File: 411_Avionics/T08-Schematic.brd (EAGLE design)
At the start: 61.7 x 25.4 mm, 41 parts, among them IC1 BQ24022, J1 USB-MICROB, J3 JST-PH-2-SMT-RA, U1 LP5907, U2 M25P10-AVMN6TP_TR, U3 LSM9DS0, U5 LTC1998, U6 ATMEGA32U4-AU, X1 8MHz

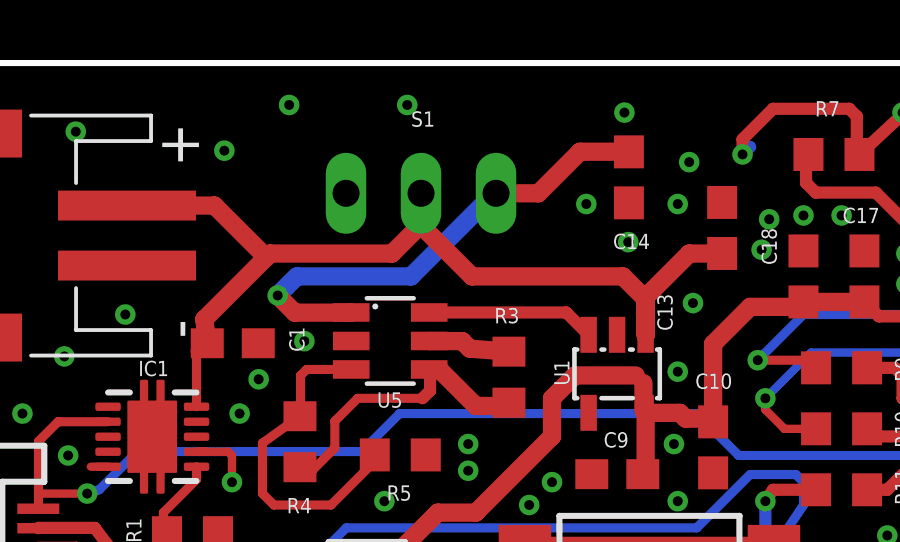
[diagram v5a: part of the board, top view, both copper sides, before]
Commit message: Updated a few oopsies on board layout.  A couple nodes not connected, switch on bottom layer.  Added a couple more vias as well.
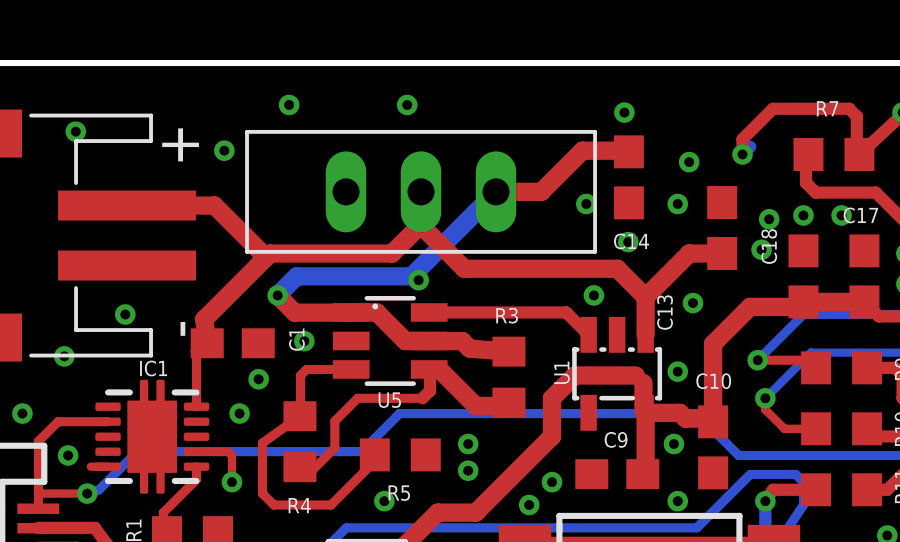
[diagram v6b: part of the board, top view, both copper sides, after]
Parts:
- flipped S1 to the top, turned to 0 degrees
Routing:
- net N$15: track 19.2 -> 22.2 mm
- net GND: vias 78 -> 80
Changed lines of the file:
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@@
 <layers>
 <layer number="1" name="Top" color="4" fill="1" visible="yes" active="yes"/>
-<layer number="16" name="Bottom" color="1" fill="1" visible="yes" active="yes"/>
+<layer number="16" name="Bottom" color="1" fill="1" visible="no" active="yes"/>
 <layer number="17" name="Pads" color="2" fill="1" visible="yes" active="yes"/>
 <layer number="18" name="Vias" color="2" fill="1" visible="yes" active="yes"/>
@@
 <layer number="20" name="Dimension" color="15" fill="1" visible="yes" active="yes"/>
 <layer number="21" name="tPlace" color="7" fill="1" visible="yes" active="yes"/>
-<layer number="22" name="bPlace" color="7" fill="1" visible="yes" active="yes"/>
+<layer number="22" name="bPlace" color="7" fill="1" visible="no" active="yes"/>
 <layer number="23" name="tOrigins" color="15" fill="1" visible="yes" active="yes"/>
-<layer number="24" name="bOrigins" color="15" fill="1" visible="yes" active="yes"/>
+<layer number="24" name="bOrigins" color="15" fill="1" visible="no" active="yes"/>
 <layer number="25" name="tNames" color="7" fill="1" visible="no" active="yes"/>
 <layer number="26" name="bNames" color="7" fill="1" visible="no" active="yes"/>
@@
 <layer number="50" name="dxf" color="7" fill="1" visible="no" active="no"/>
 <layer number="51" name="tDocu" color="7" fill="1" visible="yes" active="yes"/>
-<layer number="52" name="bDocu" color="7" fill="1" visible="yes" active="yes"/>
+<layer number="52" name="bDocu" color="7" fill="1" visible="no" active="yes"/>
 <layer number="53" name="tGND_GNDA" color="7" fill="9" visible="no" active="no"/>
 <layer number="54" name="bGND_GNDA" color="1" fill="9" visible="no" active="no"/>
@@
 <attribute name="NAME" x="34.29" y="15.605" size="0.508" layer="25" rot="R270"/>
 </element>
-<element name="S1" library="tinyav-lib" package="ESWITCH" value="COM-00102" x="18.494" y="21.058" smashed="yes" rot="MR180">
-<attribute name="NAME" x="18.161" y="23.279" size="0.508" layer="25" font="vector"/>
+<element name="S1" library="tinyav-lib" package="ESWITCH" value="COM-00102" x="18.494" y="21.106" smashed="yes">
+<attribute name="NAME" x="18.161" y="18.885" size="0.508" layer="26" font="vector" rot="MR180"/>
 </element>
 <element name="S2" library="switch-ck" package="PTS645-SMD" value="PTS645SM43SMTR92" x="26.108" y="7.056" smashed="yes" rot="R180">
@@
 <via x="27.432" y="22.098" extent="1-16" drill="0.3302"/>
 <via x="25.4" y="19.431" extent="1-16" drill="0.3302"/>
+<via x="18.415" y="18.161" extent="1-16" drill="0.3302"/>
+<via x="24.257" y="17.653" extent="1-16" drill="0.3302"/>
 </signal>
 <signal name="N$4">
@@
 <wire x1="11.608" y1="20.65" x2="13.335" y2="18.923" width="0.6096" layer="1"/>
 <wire x1="11.011" y1="13.944" x2="11.011" y2="15.803" width="0.3048" layer="1"/>
-<wire x1="17.526" y1="19.05" x2="18.542" y2="20.066" width="0.6096" layer="1"/>
-<wire x1="18.542" y1="20.066" x2="18.542" y2="21.01" width="0.6096" layer="1"/>
-<wire x1="18.542" y1="21.01" x2="18.494" y2="21.058" width="0.6096" layer="1"/>
-<wire x1="18.542" y1="20.066" x2="18.542" y2="19.939" width="0.6096" layer="1"/>
-<wire x1="18.542" y1="19.939" x2="20.193" y2="18.288" width="0.6096" layer="1"/>
-<wire x1="20.193" y1="18.288" x2="25.222" y2="18.288" width="0.6096" layer="1"/>
-<wire x1="25.222" y1="18.288" x2="25.983" y2="17.527" width="0.6096" layer="1"/>
-<wire x1="25.983" y1="17.527" x2="25.983" y2="16.343" width="0.6096" layer="1"/>
-<wire x1="25.983" y1="16.343" x2="25.98" y2="16.34" width="0.6096" layer="1"/>
 <wire x1="25.98" y1="16.34" x2="25.98" y2="17.598" width="0.6096" layer="1"/>
 <wire x1="25.98" y1="17.598" x2="27.432" y2="19.05" width="0.6096" layer="1"/>
 <wire x1="27.432" y1="19.05" x2="28.53" y2="19.05" width="0.6096" layer="1"/>
 <wire x1="28.53" y1="19.05" x2="28.532" y2="19.052" width="0.6096" layer="1"/>
+<wire x1="18.494" y1="21.106" x2="18.494" y2="20.018" width="0.6096" layer="1"/>
+<wire x1="18.494" y1="20.018" x2="17.526" y2="19.05" width="0.6096" layer="1"/>
+<wire x1="18.494" y1="21.106" x2="18.494" y2="19.987" width="0.6096" layer="1"/>
+<wire x1="18.494" y1="19.987" x2="19.939" y2="18.542" width="0.6096" layer="1"/>
+<wire x1="19.939" y1="18.542" x2="25.036" y2="18.542" width="0.6096" layer="1"/>
+<wire x1="25.036" y1="18.542" x2="25.98" y2="17.598" width="0.6096" layer="1"/>
 </signal>
 <signal name="N$12">
@@
 <wire x1="19.866" y1="16.132" x2="18.772" y2="16.132" width="0.6096" layer="1"/>
 <wire x1="18.772" y1="16.132" x2="18.768" y2="16.136" width="0.6096" layer="1"/>
-<wire x1="20.994" y1="21.058" x2="20.931" y2="21.058" width="0.6096" layer="16"/>
-<wire x1="20.931" y1="21.058" x2="18.161" y2="18.288" width="0.6096" layer="16"/>
-<wire x1="18.161" y1="18.288" x2="14.351" y2="18.288" width="0.6096" layer="16"/>
+<wire x1="18.176" y1="18.288" x2="14.351" y2="18.288" width="0.6096" layer="16"/>
 <wire x1="14.351" y1="18.288" x2="13.716" y2="17.653" width="0.6096" layer="16"/>
 <via x="13.716" y="17.653" extent="1-16" drill="0.3302"/>
@@
 <wire x1="14.284" y1="17.08" x2="16.162" y2="17.08" width="0.6096" layer="1"/>
 <wire x1="16.162" y1="17.08" x2="16.168" y2="17.086" width="0.6096" layer="1"/>
-<wire x1="20.994" y1="21.058" x2="22.406" y2="21.058" width="0.6096" layer="1"/>
-<wire x1="22.406" y1="21.058" x2="23.792" y2="22.444" width="0.6096" layer="1"/>
-<wire x1="23.792" y1="22.444" x2="25.419" y2="22.444" width="0.6096" layer="1"/>
 <wire x1="25.419" y1="22.444" x2="25.423" y2="22.44" width="0.6096" layer="1"/>
-<wire x1="18.161" y1="18.288" x2="18.772" y2="16.132" width="0" layer="19" extent="1-16"/>
+<wire x1="18.772" y1="16.132" x2="17.975" y2="16.132" width="0.6096" layer="1"/>
+<wire x1="17.975" y1="16.132" x2="17.02" y2="17.087" width="0.6096" layer="1"/>
+<wire x1="17.02" y1="17.087" x2="16.169" y2="17.087" width="0.6096" layer="1"/>
+<wire x1="16.169" y1="17.087" x2="16.168" y2="17.086" width="0.6096" layer="1"/>
+<wire x1="20.994" y1="21.106" x2="22.503" y2="21.106" width="0.6096" layer="1"/>
+<wire x1="22.503" y1="21.106" x2="23.876" y2="22.479" width="0.6096" layer="1"/>
+<wire x1="23.876" y1="22.479" x2="25.384" y2="22.479" width="0.6096" layer="1"/>
+<wire x1="25.384" y1="22.479" x2="25.423" y2="22.44" width="0.6096" layer="1"/>
+<wire x1="18.176" y1="18.288" x2="20.994" y2="21.106" width="0.6096" layer="16"/>
 </signal>
 <signal name="RED_LED">

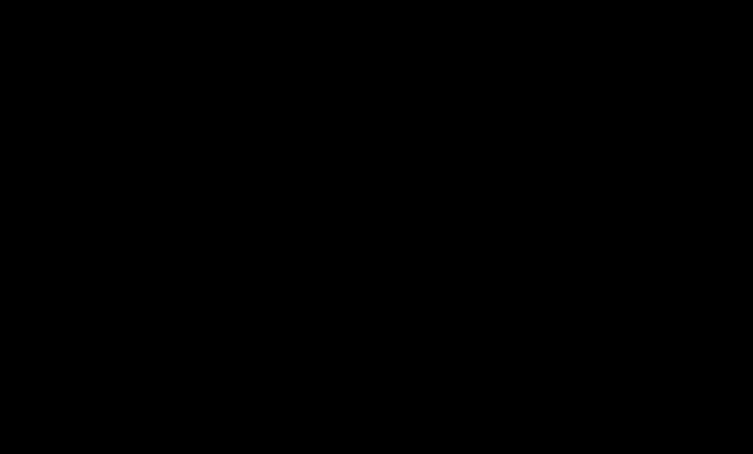
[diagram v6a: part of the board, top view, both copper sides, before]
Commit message: Added 3-pin pad for firing circuit
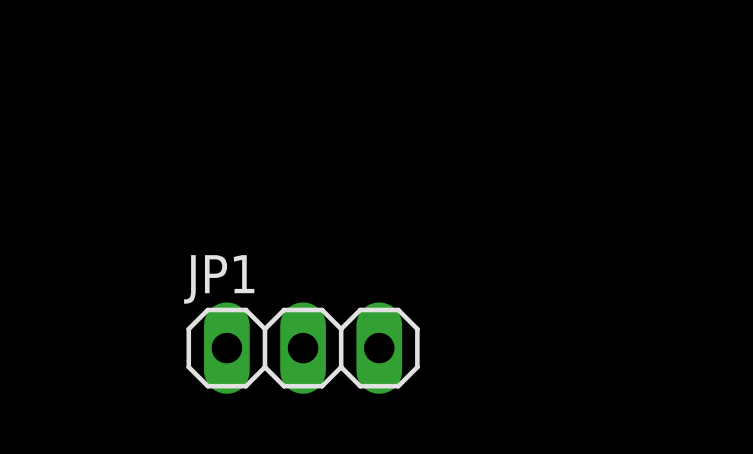
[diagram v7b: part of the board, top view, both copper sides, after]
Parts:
- added JP1: (no value), pinhead:1X03
- R6, R8: value 150 -> 330
- R7: value 100 -> 330
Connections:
- new net FIRE_EN: JP1.2, U6.37
- net GND: now also JP1.3
- net VCC: now also JP1.1

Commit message: Kind of ugly, but I got the ignition switch hooked up.
Should work alright!  Board is ready to be shipped off!
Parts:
- moved JP1 55.4 mm to (60.1, 7.11), turned to 90 degrees
- moved C11 0.90 mm to (50.4, 7.94)
- moved X1 0.64 mm to (54.3, 6.63)
- moved C12 0.36 mm to (50.3, 4.56)
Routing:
- net FIRE_EN: track 0.00 -> 30.4 mm, vias 0 -> 3
- net VCC: track 99.0 -> 121.3 mm
- net MOSI: track 67.5 -> 69.3 mm
- net GYR_EN: track 26.7 -> 27.9 mm
- net XM_EN: track 28.1 -> 28.9 mm
- net GND: vias 80 -> 99
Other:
- board size 61.7 x 25.4 mm -> 63.1 x 25.4 mm
